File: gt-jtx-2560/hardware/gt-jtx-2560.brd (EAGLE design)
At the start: 100 x 80 mm, 21 parts

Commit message: added new files
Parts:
- removed LCD1: LCD-G12864-BARE, SparkFun-Displays:1X20
- added J1: (no value), SparkFun-Connectors:1X20
- added R1: 2.2K, resistor:0204/5
- added R2: 1K, resistor:0204/5
- added ROT_1, ROT_2: rgSbVBCA, Rembrandt Electronics - JST XH Connectors v1-0:JST-XH-08-PACKAGE-LONG-PAD
- moved SD 2.54 mm to (34.3, 27.9)
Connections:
- removed net A: LCD1.19
- removed net K: LCD1.20
- removed net VDD: LCD1.1
- removed net VSS: LCD1.2
- new net N$31: B1.15, ROT_1.3
- new net N$47: B1.14, ROT_2.3
- new net N$48: B1.2, ROT_1.8
- new net N$49: B1.3, ROT_1.6
- new net N$50: B1.19, ROT_2.8
- new net N$51: B1.18, ROT_2.6
- new net N$52: J1.19, R1.1
- new net N$53: B1.30, J1.6
- new net N$54: B1.31, J1.16
- new net N$55: B1.32, J1.4
- new net N$56: B1.33, J1.17
- new net N$57: B1.34, J1.15
- new net N$58: J1.5, R2.1
- net N$1: now also J1.7; no longer LCD1.4
- net N$2: now also J1.8; no longer LCD1.5
- net N$3: now also J1.9; no longer LCD1.6
- net N$4: now also J1.10; no longer LCD1.7
- net N$43: now also J1.1, J1.20, R2.2, ROT_1.7, ROT_2.7
- net N$44: now also J1.2, R1.2, ROT_1.5, ROT_2.5
- net N$5: now also J1.11; no longer LCD1.8
- net N$6: now also J1.12; no longer LCD1.9
- net N$7: now also J1.13; no longer LCD1.10
- net N$8: now also J1.14; no longer LCD1.11
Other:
- board size 100 x 80 mm -> 101.3 x 80 mm

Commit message: added case design, changed the schematic for lcd
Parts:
- added ID1, ID2: (no value), Rembrandt Electronics - JST XH Connectors v1-0:JST-XH-03-PACKAGE-LONG-PAD
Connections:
- removed net N$43: AIL.3, AIL_DR.3, B1.GND@0, B1.GND@1, B1.GND@2, B1.GND@3, B1.GND@4, ELE.3, ELE_DR.3, GEAR.3, H_B.3, J1.1, J1.20, NAVI.8, POT1.3, POT2.3, POT3.3, PPM.3, R2.2, ROT_1.7, ROT_2.7, RUD.3, RUD_DR.3, SD.6, THR.3, THR_X.3, TRIML.8, TRIMR.8, TRN.3
- removed net N$44: AIL.1, AIL_DR.1, B1.5V@0, B1.AREF, ELE.1, ELE_DR.1, GEAR.1, J1.2, NAVI.1, POT1.1, POT2.1, POT3.1, PPM.2, R1.2, ROT_1.5, ROT_2.5, RUD.1, RUD_DR.1, SD.5, THR.1, THR_X.1, TRIML.1, TRIMR.1, TRN.1
- new net GND: AIL.3, AIL_DR.3, B1.GND@0, B1.GND@1, B1.GND@2, B1.GND@3, B1.GND@4, ELE.3, ELE_DR.3, GEAR.3, H_B.3, ID1.3, ID2.3, J1.1, J1.20, NAVI.8, POT1.3, POT2.3, POT3.3, PPM.3, R2.2, ROT_1.7, ROT_2.7, RUD.3, RUD_DR.3, SD.6, THR.3, THR_X.3, TRIML.8, TRIMR.8, TRN.3
- new net N$59: B1.36, ID2.2
- new net N$60: B1.37, ID1.2
- new net VCC: AIL.1, AIL_DR.1, B1.5V@0, B1.AREF, ELE.1, ELE_DR.1, GEAR.1, ID1.1, ID2.1, J1.2, NAVI.1, POT1.1, POT2.1, POT3.1, PPM.2, R1.2, ROT_1.5, ROT_2.5, RUD.1, RUD_DR.1, SD.5, THR.1, THR_X.1, TRIML.1, TRIMR.1, TRN.1
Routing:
- net GND: track 0.00 -> 321.6 mm
- net VCC: track 0.00 -> 315.7 mm
- net N$18: track 0.00 -> 101.4 mm, vias 0 -> 1
- net N$16: track 0.00 -> 64.7 mm
- net N$30: track 0.00 -> 58.6 mm
- net N$15: track 0.00 -> 55.5 mm
- net N$26: track 0.00 -> 54.9 mm
- net N$29: track 0.00 -> 51.9 mm
- net N$51: track 0.00 -> 48.8 mm
- net N$39: track 0.00 -> 44.4 mm
- net N$55: track 0.00 -> 41.6 mm
- net N$50: track 0.00 -> 39.0 mm
- net N$45: track 0.00 -> 38.4 mm, vias 0 -> 1
- net N$47: track 0.00 -> 38.3 mm, vias 0 -> 1
- net N$31: track 0.00 -> 36.8 mm
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- added copper zone on layer 1, net GND
- added copper zone on layer 16, net GND
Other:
- board text added: "gt-jtx m2560"
- board text added: "www.gluedtomatoes.com"

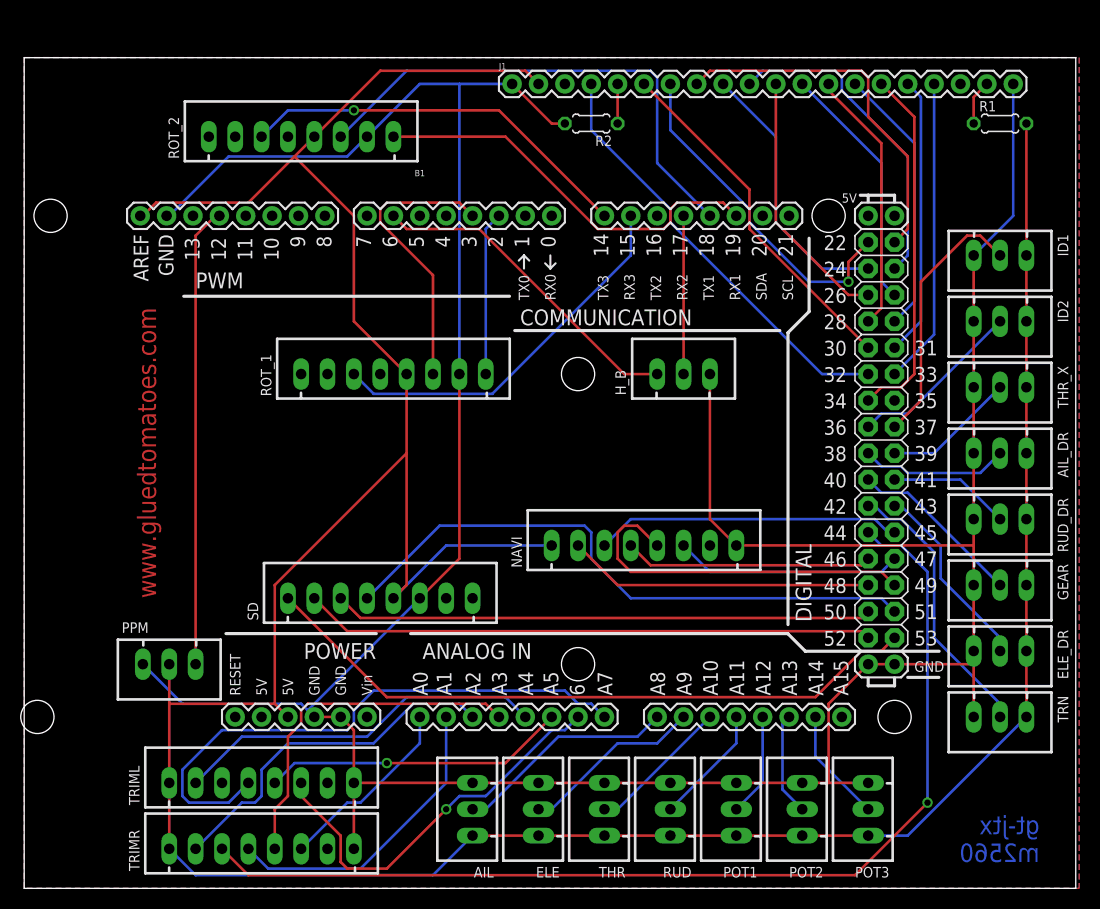
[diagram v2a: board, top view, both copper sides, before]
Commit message: fixed LCD connections and added connector for contrast adjustment
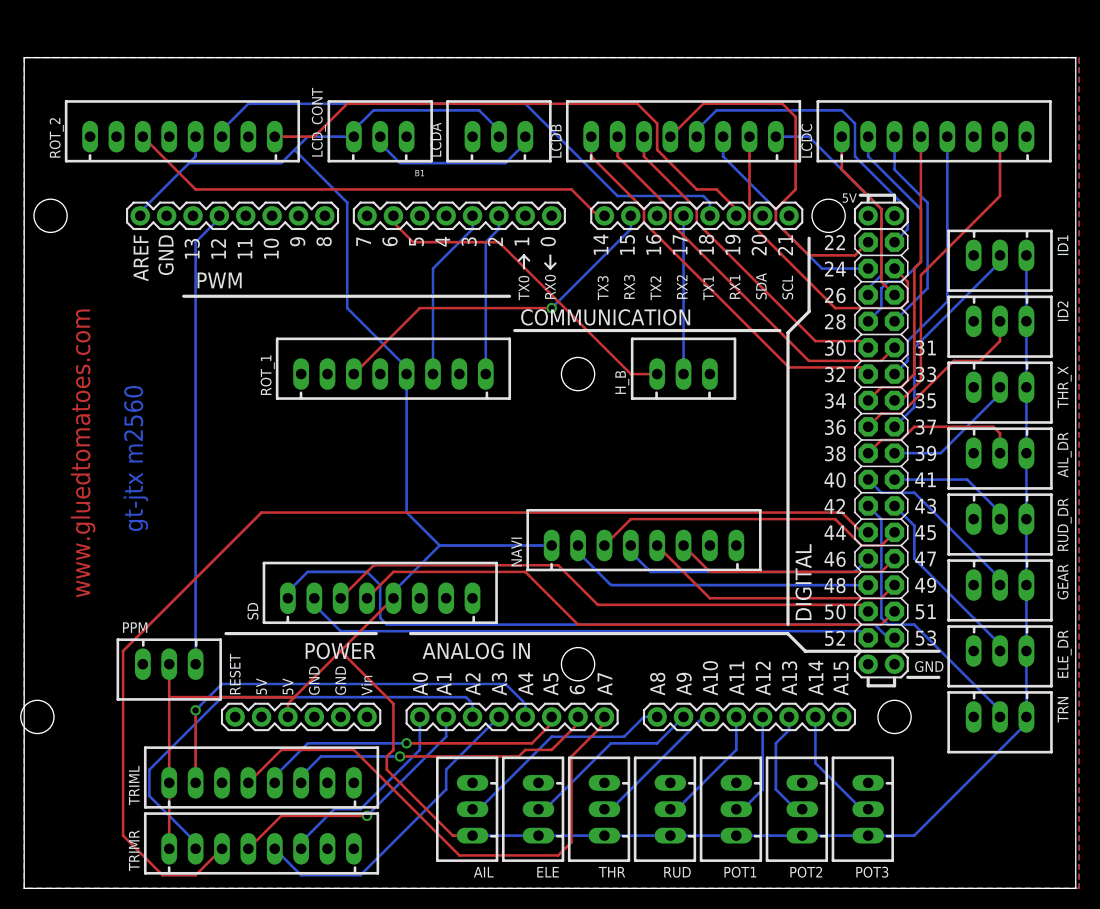
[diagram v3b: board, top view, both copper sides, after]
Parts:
- removed J1: (no value), SparkFun-Connectors:1X20
- removed R1: 2.2K, resistor:0204/5
- removed R2: 1K, resistor:0204/5
- added LCDA: LCD, Rembrandt Electronics - JST XH Connectors v1-0:JST-XH-03-PACKAGE-LONG-PAD
- added LCDB, LCDC: LCD, Rembrandt Electronics - JST XH Connectors v1-0:JST-XH-08-PACKAGE-LONG-PAD
- added LCD_CONT: LCD_CONT, Rembrandt Electronics - JST XH Connectors v1-0:JST-XH-03-PACKAGE-LONG-PAD
- moved ROT_2 11.4 mm to (15.2, 72.4)
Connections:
- removed net N$57: B1.34, J1.15
- removed net N$58: J1.5, R2.1
- new net N$43: B1.30, LCDB.3
- new net N$44: B1.31, LCDB.2
- net GND: now also LCDA.1, LCDC.8, LCD_CONT.3; no longer J1.1, J1.20, R2.2
- net N$1: now also LCDB.4; no longer J1.7
- net N$2: now also LCDB.5; no longer J1.8
- net N$3: now also LCDB.6; no longer J1.9
- net N$4: now also LCDB.7; no longer J1.10
- net N$5: now also LCDB.8; no longer J1.11
- net N$52: now also B1.32, LCDB.1; no longer J1.19, R1.1
- net N$53: now also B1.34, LCDC.4; no longer B1.30, J1.6
- net N$54: now also B1.33, LCDC.5; no longer B1.31, J1.16
- net N$55: now also B1.35, LCDC.7; no longer B1.32, J1.4
- net N$56: now also LCDA.3, LCD_CONT.2; no longer B1.33, J1.17
- net N$6: now also LCDC.1; no longer J1.12
- net N$7: now also LCDC.2; no longer J1.13
- net N$8: now also LCDC.3; no longer J1.14
- net VCC: now also LCDA.2, LCD_CONT.1; no longer J1.2, R1.2
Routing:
- net GND: track 321.6 -> 0.00 mm
- net N$44: track 0.00 -> 38.0 mm
- net VCC: track 315.7 -> 279.0 mm
- net N$57: track 34.8 -> 0.00 mm
- net N$52: track 4.34 -> 38.0 mm
- net N$43: track 0.00 -> 31.9 mm
- net N$50: track 39.0 -> 52.1 mm
- net N$56: track 29.5 -> 16.8 mm
- net N$55: track 41.6 -> 30.0 mm
- net N$49: track 27.7 -> 16.8 mm
- net N$14: track 34.5 -> 45.0 mm
- net N$12: track 35.1 -> 25.5 mm
- net N$47: track 38.3 -> 47.6 mm, vias 1 -> 0
- net N$45: track 38.4 -> 30.0 mm
- net N$6: track 24.0 -> 17.3 mm
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
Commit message: added sim connector
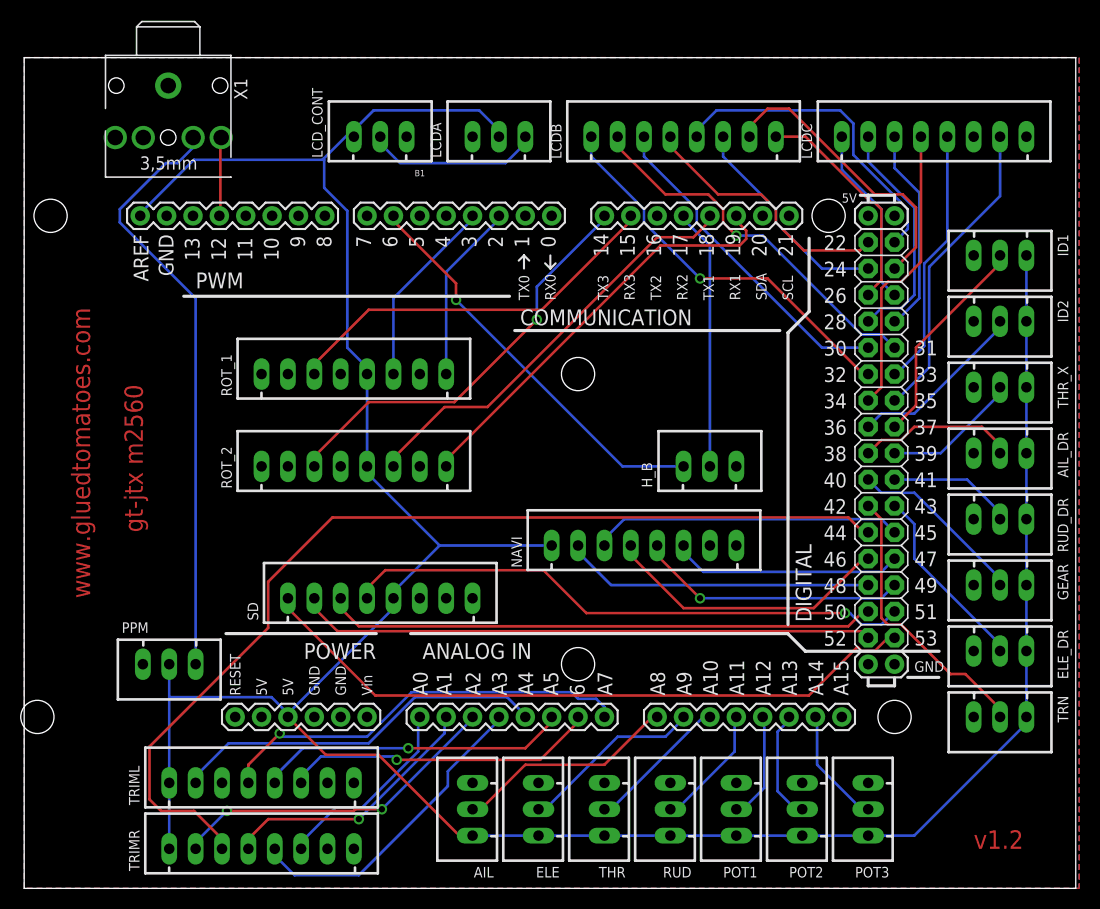
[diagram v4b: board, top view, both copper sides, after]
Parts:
- added X1: SIM, adafruit:STX3100
- moved ROT_2 35.8 mm to (31.8, 40.6)
- moved H_B 9.25 mm to (66.0, 40.6)
- moved ROT_1 3.81 mm to (31.8, 49.5)
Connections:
- new net N$57: PPM.1, X1.3
- net GND: now also X1.1
- net N$39: now also X1.2; no longer PPM.1
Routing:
- net N$57: track 0.00 -> 57.3 mm
- net N$39: track 44.5 -> 7.67 mm
- net N$51: track 53.9 -> 41.2 mm
- net N$14: track 45.0 -> 32.4 mm, vias 0 -> 2
- net N$18: track 108.0 -> 96.1 mm
- net N$50: track 52.1 -> 41.0 mm
- net N$1: track 35.6 -> 25.2 mm
- net N$41: track 15.2 -> 25.2 mm
- net N$15: track 50.5 -> 40.7 mm, vias 0 -> 1
- net N$47: track 47.6 -> 40.5 mm, vias 0 -> 1
- net N$32: track 32.1 -> 39.1 mm, vias 0 -> 1
- net VCC: track 279.0 -> 272.4 mm
- net N$46: track 41.8 -> 36.4 mm, vias 1 -> 0
- net N$31: track 33.7 -> 37.6 mm, vias 1 -> 0
- net N$11: track 24.8 -> 27.9 mm
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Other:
- board text added: "v1.2"
